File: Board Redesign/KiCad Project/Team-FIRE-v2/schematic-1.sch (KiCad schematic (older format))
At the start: 32 parts, among them J1 SIM_Card, J2 53885-0408, U1 TPS40210DGQR, U2 NCN4555MN, U3 CSD18543Q3A

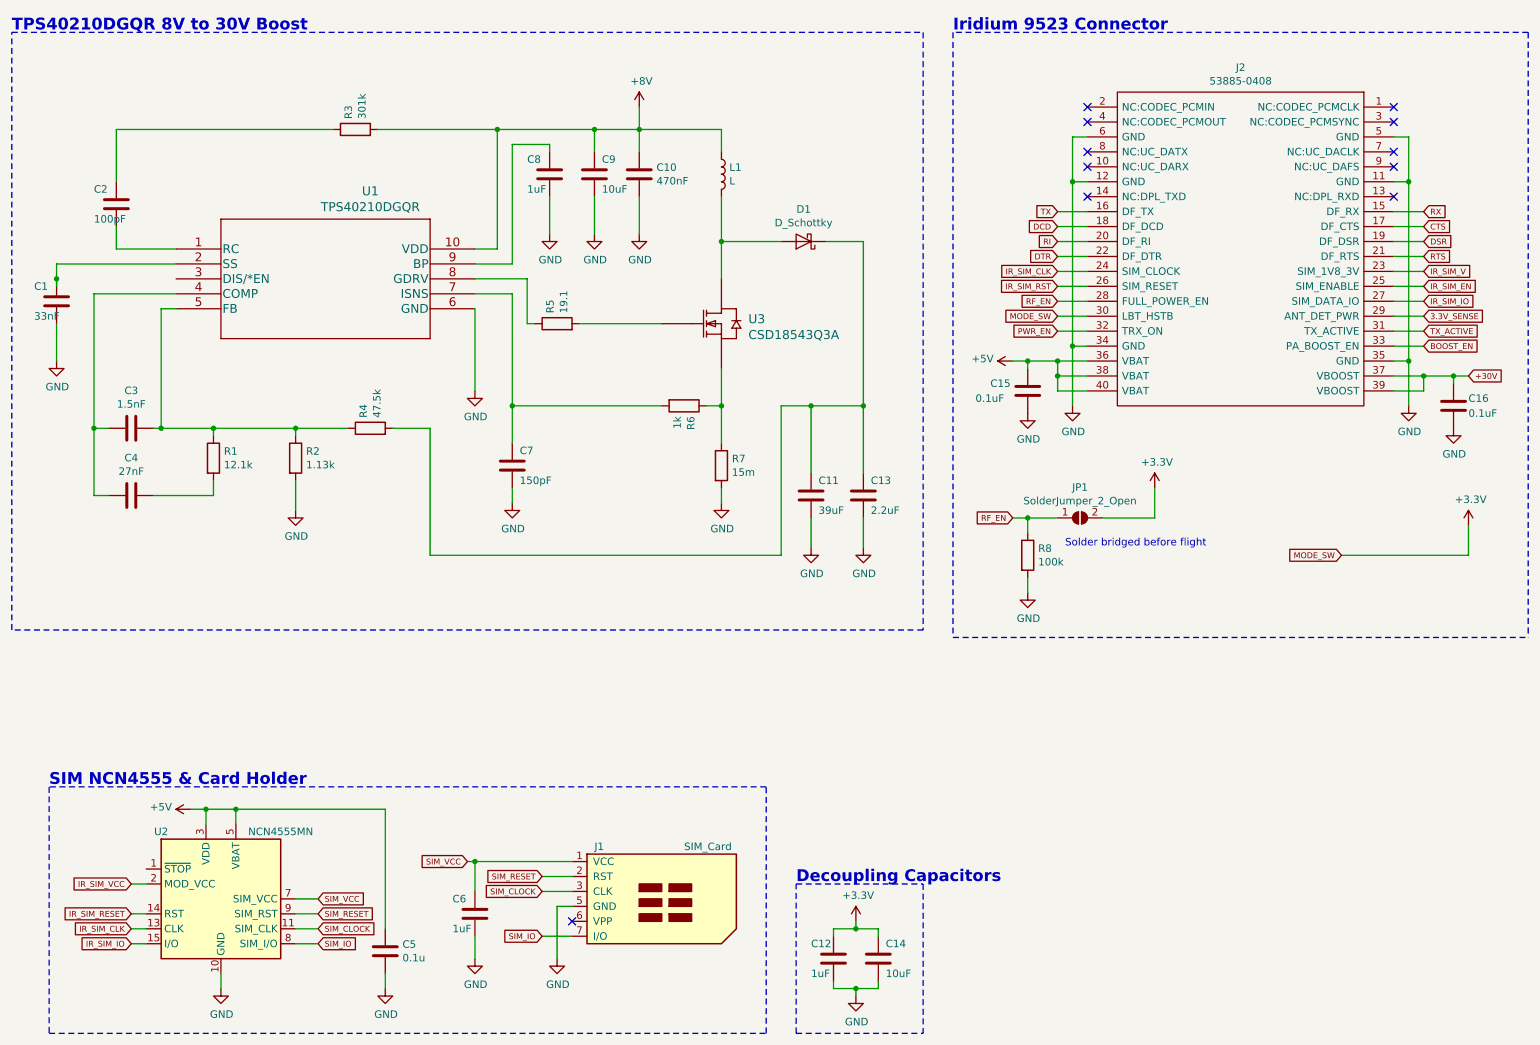
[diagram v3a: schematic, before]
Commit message: Progress
- Corrected many footprint errors on components
- Finalized work on schematic 3
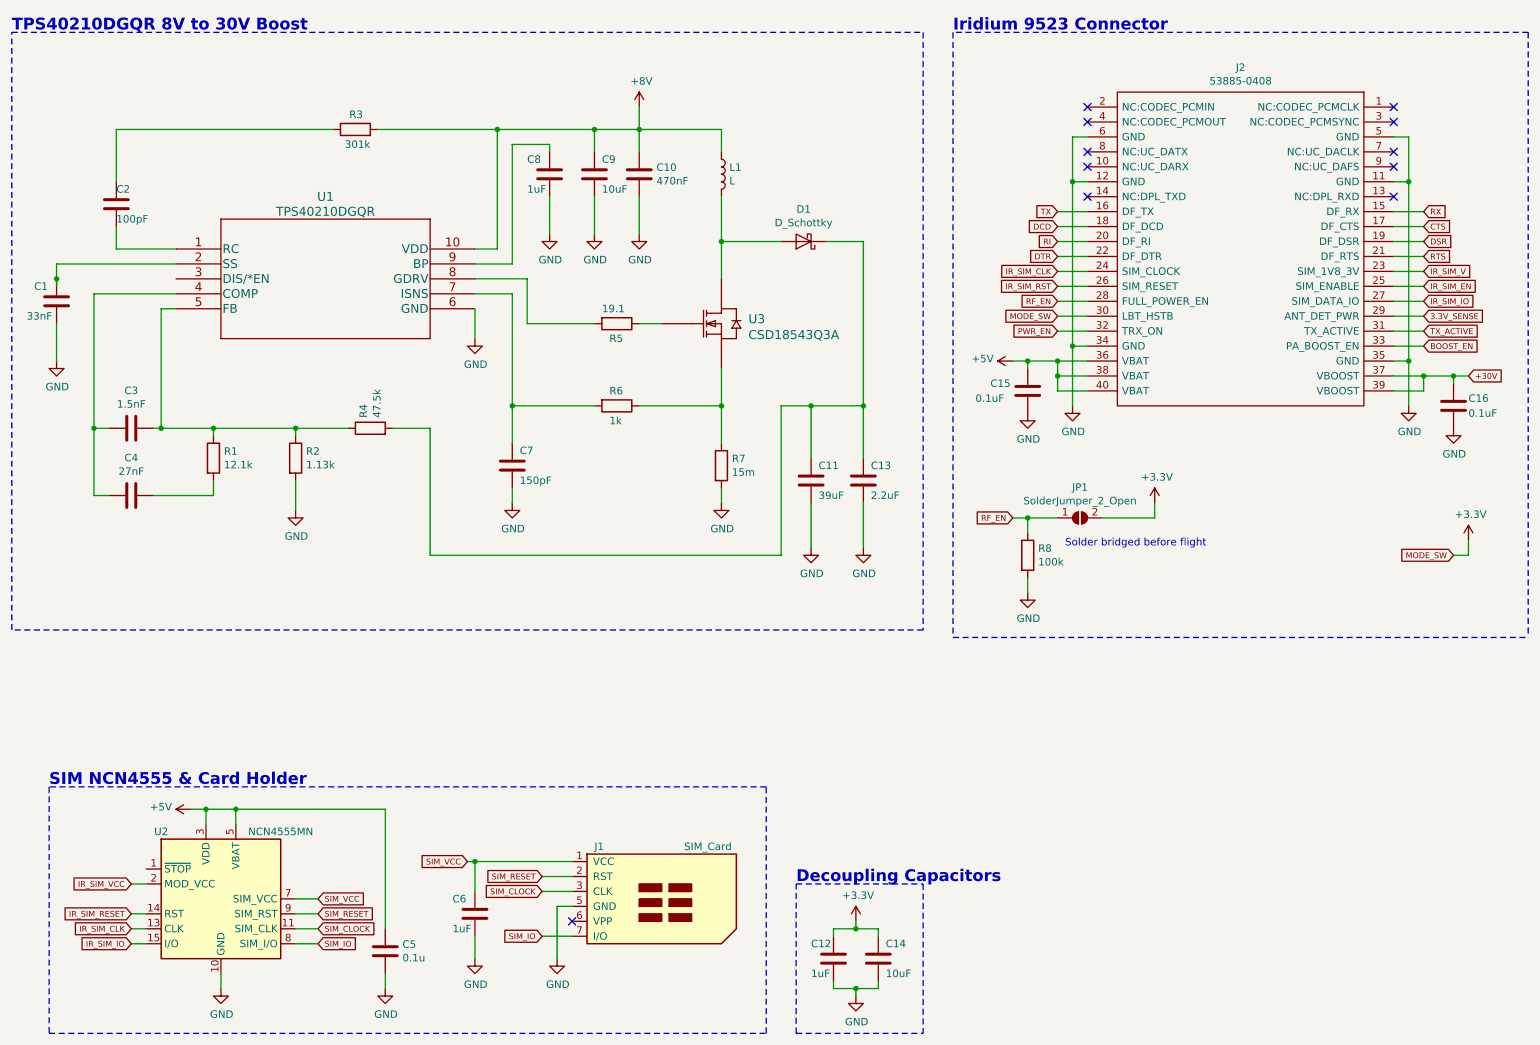
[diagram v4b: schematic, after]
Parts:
- C1, C11, C12, C13, C14, C2, C7, C8, C9: footprint Inductor_SMD:L_0603_1608Metric -> Capacitor_SMD:C_0603_1608Metric
- C10: footprint (none) -> Capacitor_SMD:C_0603_1608Metric
- J1: footprint (none) -> Package_DFN_QFN:QFN-16-1EP_3x3mm_P0.5mm_EP1.75x1.75mm
- JP1: footprint (none) -> Jumper:SolderJumper-2_P1.3mm_Open_Pad1.0x1.5mm
- R6, R8: footprint (none) -> Resistor_SMD:R_0603_1608Metric
- U2: MPN (none) -> NCN4555MNR2G
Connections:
- net at R5.1: now also U3.4 (G); no longer U1.8 (GDRV)
- net at R5.2: now also U1.8 (GDRV); no longer U3.4 (G)
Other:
- moved on the sheet: C11, C13, R5, R6
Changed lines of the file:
@@
 F 0 "J1" H 4650 7050 50  0000 L CNN
 F 1 "SIM_Card" H 5250 7050 50  0000 L CNN
-F 2 "" H 5000 7000 50  0001 C CNN
+F 2 "Package_DFN_QFN:QFN-16-1EP_3x3mm_P0.5mm_EP1.75x1.75mm" H 5000 7000 50  0001 C CNN
 F 3 " ~" H 4950 6650 50  0001 C CNN
 	1    5000 6650
@@
 F 2 "Package_DFN_QFN:QFN-16-1EP_3x3mm_P0.5mm_EP1.75x1.75mm" H 3450 6150 50  0001 C CNN
 F 3 "https://www.onsemi.com/pub/Collateral/NCN4555-D.PDF" H 550 6400 50  0001 C CNN
+F 4 "NCN4555MNR2G" H 2150 6600 50  0001 C CNN "MPN"
 	1    2150 6600
 	1    0    0    -1
@@
 F 0 "JP1" H 7900 4255 50  0000 C CNN
 F 1 "SolderJumper_2_Open" H 7900 4164 50  0000 C CNN
-F 2 "" H 7900 4050 50  0001 C CNN
+F 2 "Jumper:SolderJumper-2_P1.3mm_Open_Pad1.0x1.5mm" H 7900 4050 50  0001 C CNN
 F 3 "~" H 7900 4050 50  0001 C CNN
 	1    7900 4050
@@
 RF_EN
 Wire Wire Line
-	8400 3850 8400 4050
-Wire Wire Line
 	8400 4050 8050 4050
 $Comp
 L power:+3.3V #PWR0109
 U 1 1 5E5C1CAF
-P 8400 3850
+P 8400 3950
 AR Path="/5E4D0D8F/5E5C1CAF" Ref="#PWR0109"  Part="1"
 AR Path="/5E759307/5E5C1CAF" Ref="#PWR?"  Part="1"
-F 0 "#PWR0109" H 8400 3700 50  0001 C CNN
-F 1 "+3.3V" H 8415 4023 50  0000 C CNN
-F 2 "" H 8400 3850 50  0001 C CNN
-F 3 "" H 8400 3850 50  0001 C CNN
-	1    8400 3850
-	1    0    0    -1
-$EndComp
-Text GLabel 9650 4300 0    39   Input ~ 0
+F 0 "#PWR0109" H 8400 3800 50  0001 C CNN
+F 1 "+3.3V" H 8415 4123 50  0000 C CNN
+F 2 "" H 8400 3950 50  0001 C CNN
+F 3 "" H 8400 3950 50  0001 C CNN
+	1    8400 3950
+	1    0    0    -1
+$EndComp
+Text GLabel 10400 4300 0    39   Input ~ 0
 MODE_SW
-Wire Wire Line
-	10500 4300 9650 4300
 $Comp
 L power:+3.3V #PWR0110
 U 1 1 5E5C8ABA
-P 10500 4100
+P 10500 4200
 AR Path="/5E4D0D8F/5E5C8ABA" Ref="#PWR0110"  Part="1"
 AR Path="/5E759307/5E5C8ABA" Ref="#PWR?"  Part="1"
-F 0 "#PWR0110" H 10500 3950 50  0001 C CNN
-F 1 "+3.3V" H 10515 4273 50  0000 C CNN
-F 2 "" H 10500 4100 50  0001 C CNN
-F 3 "" H 10500 4100 50  0001 C CNN
-	1    10500 4100
-	1    0    0    -1
-$EndComp
-Wire Wire Line
-	10500 4100 10500 4300
+F 0 "#PWR0110" H 10500 4050 50  0001 C CNN
+F 1 "+3.3V" H 10515 4373 50  0000 C CNN
+F 2 "" H 10500 4200 50  0001 C CNN
+F 3 "" H 10500 4200 50  0001 C CNN
+	1    10500 4200
+	1    0    0    -1
+$EndComp
 Text Notes 7800 4250 0    50   ~ 0
 Solder bridged before flight
@@
 F 0 "R8" H 7620 4346 50  0000 L CNN
 F 1 "100k" H 7620 4255 50  0000 L CNN
-F 2 "" V 7480 4300 50  0001 C CNN
+F 2 "Resistor_SMD:R_0603_1608Metric" V 7480 4300 50  0001 C CNN
 F 3 "~" H 7550 4300 50  0001 C CNN
 	1    7550 4300
@@
 F 0 "C12" H 6100 7100 50  0000 L CNN
 F 1 "1uF" H 6100 6900 50  0000 L CNN
-F 2 "Inductor_SMD:L_0603_1608Metric" H 6288 6850 50  0001 C CNN
+F 2 "Capacitor_SMD:C_0603_1608Metric" H 6288 6850 50  0001 C CNN
 F 3 "~" H 6250 7000 50  0001 C CNN
 	1    6250 7000
@@
 F 0 "C14" H 6600 7100 50  0000 L CNN
 F 1 "10uF" H 6600 6900 50  0000 L CNN
-F 2 "Inductor_SMD:L_0603_1608Metric" H 6588 6850 50  0001 C CNN
+F 2 "Capacitor_SMD:C_0603_1608Metric" H 6588 6850 50  0001 C CNN
 F 3 "~" H 6550 7000 50  0001 C CNN
 	1    6550 7000
@@
 F 0 "C9" H 4700 1850 50  0000 L CNN
 F 1 "10uF" H 4700 1650 50  0000 L CNN
-F 2 "Inductor_SMD:L_0603_1608Metric" H 4688 1600 50  0001 C CNN
+F 2 "Capacitor_SMD:C_0603_1608Metric" H 4688 1600 50  0001 C CNN
 F 3 "~" H 4650 1750 50  0001 C CNN
 	1    4650 1750
@@
 U 1 1 5EA803DA
 P 1450 1950
-F 0 "C2" H 1300 2050 50  0000 L CNN
-F 1 "100pF" H 1300 1850 50  0000 L CNN
-F 2 "Inductor_SMD:L_0603_1608Metric" H 1488 1800 50  0001 C CNN
+F 0 "C2" H 1450 2050 50  0000 L CNN
+F 1 "100pF" H 1450 1850 50  0000 L CNN
+F 2 "Capacitor_SMD:C_0603_1608Metric" H 1488 1800 50  0001 C CNN
 F 3 "~" H 1450 1950 50  0001 C CNN
 	1    1450 1950
@@
 P 1050 2600
 F 0 "C1" H 900 2700 50  0000 L CNN
-F 1 "33nF" H 900 2500 50  0000 L CNN
-F 2 "Inductor_SMD:L_0603_1608Metric" H 1088 2450 50  0001 C CNN
+F 1 "33nF" H 850 2500 50  0000 L CNN
+F 2 "Capacitor_SMD:C_0603_1608Metric" H 1088 2450 50  0001 C CNN
 F 3 "~" H 1050 2600 50  0001 C CNN
 	1    1050 2600
@@
 AR Path="/5E4D0D8F/5EB0327A" Ref="R3"  Part="1"
 AR Path="/5E759307/5EB0327A" Ref="R?"  Part="1"
-F 0 "R3" H 3120 1496 50  0000 L CNN
-F 1 "301k" H 3120 1405 50  0000 L CNN
+F 0 "R3" V 3150 1400 50  0000 L CNN
+F 1 "301k" V 2950 1350 50  0000 L CNN
 F 2 "" V 2980 1450 50  0001 C CNN
 F 3 "~" H 3050 1450 50  0001 C CNN
@@
 F 0 "C8" H 4200 1850 50  0000 L CNN
 F 1 "1uF" H 4200 1650 50  0000 L CNN
-F 2 "Inductor_SMD:L_0603_1608Metric" H 4388 1600 50  0001 C CNN
+F 2 "Capacitor_SMD:C_0603_1608Metric" H 4388 1600 50  0001 C CNN
 F 3 "~" H 4350 1750 50  0001 C CNN
 	1    4350 1750
@@
 L Device:R R5
 U 1 1 5EB8AD65
-P 4400 2750
+P 4800 2750
 AR Path="/5E4D0D8F/5EB8AD65" Ref="R5"  Part="1"
 AR Path="/5E759307/5EB8AD65" Ref="R?"  Part="1"
-F 0 "R5" H 4470 2796 50  0000 L CNN
-F 1 "19.1" H 4470 2705 50  0000 L CNN
-F 2 "" V 4330 2750 50  0001 C CNN
-F 3 "~" H 4400 2750 50  0001 C CNN
-	1    4400 2750
-	0    -1   -1   0
+F 0 "R5" V 4900 2700 50  0000 L CNN
+F 1 "19.1" V 4700 2650 50  0000 L CNN
+F 2 "" V 4730 2750 50  0001 C CNN
+F 3 "~" H 4800 2750 50  0001 C CNN
+	1    4800 2750
+	0    1    1    0
 $EndComp
 $Comp
 L Device:R R6
 U 1 1 5EB90F5A
-P 5250 3300
+P 4800 3300
 AR Path="/5E4D0D8F/5EB90F5A" Ref="R6"  Part="1"
 AR Path="/5E759307/5EB90F5A" Ref="R?"  Part="1"
-F 0 "R6" H 5320 3346 50  0000 L CNN
-F 1 "1k" H 5320 3255 50  0000 L CNN
-F 2 "" V 5180 3300 50  0001 C CNN
-F 3 "~" H 5250 3300 50  0001 C CNN
-	1    5250 3300
+F 0 "R6" V 4700 3250 50  0000 L CNN
+F 1 "1k" V 4900 3250 50  0000 L CNN
+F 2 "Resistor_SMD:R_0603_1608Metric" V 4730 3300 50  0001 C CNN
+F 3 "~" H 4800 3300 50  0001 C CNN
+	1    4800 3300
 	0    1    1    0
 $EndComp
@@
 F 0 "C7" H 4150 3800 50  0000 L CNN
 F 1 "150pF" H 4150 3600 50  0000 L CNN
-F 2 "Inductor_SMD:L_0603_1608Metric" H 4138 3550 50  0001 C CNN
+F 2 "Capacitor_SMD:C_0603_1608Metric" H 4138 3550 50  0001 C CNN
 F 3 "~" H 4100 3700 50  0001 C CNN
 	1    4100 3700
@@
 L power:GND #PWR0118
 U 1 1 5EB8485D
-P 3850 3200
-F 0 "#PWR0118" H 3850 2950 50  0001 C CNN
-F 1 "GND" H 3855 3027 50  0000 C CNN
-F 2 "" H 3850 3200 50  0001 C CNN
-F 3 "" H 3850 3200 50  0001 C CNN
-	1    3850 3200
+P 3850 2850
+F 0 "#PWR0118" H 3850 2600 50  0001 C CNN
+F 1 "GND" H 3855 2677 50  0000 C CNN
+F 2 "" H 3850 2850 50  0001 C CNN
+F 3 "" H 3850 2850 50  0001 C CNN
+	1    3850 2850
 	1    0    0    -1
 $EndComp
@@
 	4100 3850 4100 3950
 Wire Wire Line
-	3850 2650 3850 3200
+	3850 2650 3850 2850
 Wire Wire Line
 	3850 2550 4100 2550
@@
 	4200 2450 4200 2750
 Wire Wire Line
-	4200 2750 4250 2750
-Wire Wire Line
 	3850 2450 4200 2450
-Wire Wire Line
-	5400 3300 5500 3300
 $Comp
 L Boost_switch:CSD18543Q3A U3
@@
 F 0 "C10" H 5065 1796 50  0000 L CNN
 F 1 "470nF" H 5065 1705 50  0000 L CNN
-F 2 "" H 4988 1600 50  0001 C CNN
+F 2 "Capacitor_SMD:C_0603_1608Metric" H 4988 1600 50  0001 C CNN
 F 3 "~" H 4950 1750 50  0001 C CNN
 	1    4950 1750
@@
 	4100 3550 4100 3300
 Wire Wire Line
-	4100 3300 5100 3300
-Wire Wire Line
-	4550 2750 5100 2750
+	4100 3300 4650 3300
 $Comp
 L Boost_chip_v3:TPS40210DGQR U1
 U 1 1 5ECD905A
 P 1850 2250
-F 0 "U1" H 3150 2637 60  0000 C CNN
-F 1 "TPS40210DGQR" H 3150 2531 60  0000 C CNN
+F 0 "U1" H 2850 2600 60  0000 C CNN
+F 1 "TPS40210DGQR" H 2850 2500 60  0000 C CNN
 F 2 "DGQ10_1P88X1P57" H 3150 2490 60  0001 C CNN
 F 3 "" H 1850 2250 60  0000 C CNN
@@
 L Device:C C11
 U 1 1 5ED7F879
-P 6100 3900
-F 0 "C11" H 6150 4000 50  0000 L CNN
-F 1 "39uF" H 6150 3800 50  0000 L CNN
-F 2 "Inductor_SMD:L_0603_1608Metric" H 6138 3750 50  0001 C CNN
-F 3 "~" H 6100 3900 50  0001 C CNN
-	1    6100 3900
+P 6100 3800
+F 0 "C11" H 6150 3900 50  0000 L CNN
+F 1 "39uF" H 6150 3700 50  0000 L CNN
+F 2 "Capacitor_SMD:C_0603_1608Metric" H 6138 3650 50  0001 C CNN
+F 3 "~" H 6100 3800 50  0001 C CNN
+	1    6100 3800
 	1    0    0    -1
 $EndComp
@@
 L Device:C C13
 U 1 1 5ED8008F
-P 6450 3900
-F 0 "C13" H 6500 4000 50  0000 L CNN
-F 1 "2.2uF" H 6500 3800 50  0000 L CNN
-F 2 "Inductor_SMD:L_0603_1608Metric" H 6488 3750 50  0001 C CNN
-F 3 "~" H 6450 3900 50  0001 C CNN
-	1    6450 3900
+P 6450 3800
+F 0 "C13" H 6500 3900 50  0000 L CNN
+F 1 "2.2uF" H 6500 3700 50  0000 L CNN
+F 2 "Capacitor_SMD:C_0603_1608Metric" H 6488 3650 50  0001 C CNN
+F 3 "~" H 6450 3800 50  0001 C CNN
+	1    6450 3800
 	1    0    0    -1
 $EndComp
@@
 $EndComp
 Wire Wire Line
-	6450 4250 6450 4050
-Wire Wire Line
-	6100 4250 6100 4050
-Wire Wire Line
 	2100 3450 2650 3450
 Connection ~ 2100 3450
@@
 Wire Wire Line
 	3300 3450 3550 3450
-Wire Wire Line
-	6100 3750 6100 3300
 Wire Wire Line
 	5900 4300 3550 4300
@@
 Connection ~ 6450 3300
 Wire Wire Line
-	6450 3300 6450 3750
+	6450 3300 6450 3650
 Text Notes 750  800  0    79   ~ 16
 TPS40210DGQR 8V to 30V Boost
@@
 	0    -1   -1   0
 $EndComp
+Wire Wire Line
+	4950 3300 5500 3300
+Wire Wire Line
+	6100 3650 6100 3300
+Wire Wire Line
+	6100 3950 6100 4250
+Wire Wire Line
+	6450 3950 6450 4250
+Wire Wire Line
+	4950 2750 5100 2750
+Wire Wire Line
+	4200 2750 4650 2750
+Wire Wire Line
+	8400 3950 8400 4050
+Wire Wire Line
+	10500 4200 10500 4300
+Wire Wire Line
+	10400 4300 10500 4300
 $EndSCHEMATC
